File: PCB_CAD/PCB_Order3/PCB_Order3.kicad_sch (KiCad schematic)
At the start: 93 parts, among them J1 Conn_01x03_Socket, SW1 SLW-883935-2A-D

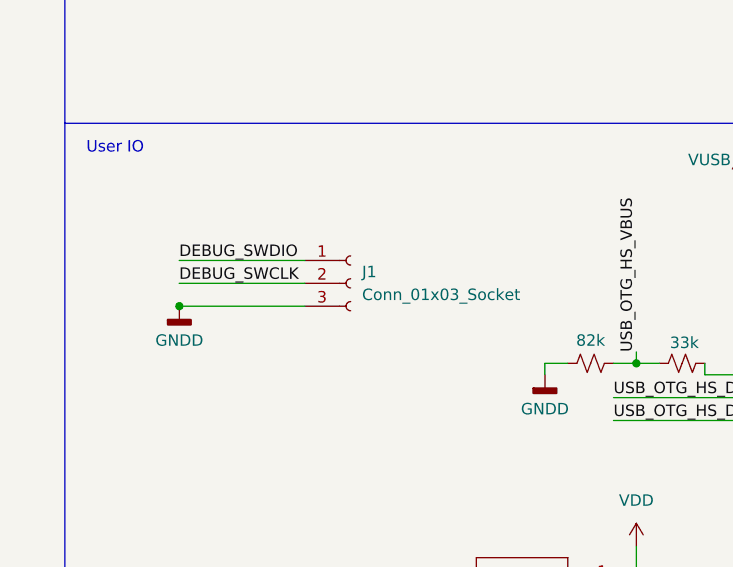
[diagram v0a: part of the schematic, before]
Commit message: preserve current PCB state, substantively ready to go to fab but messy on small details
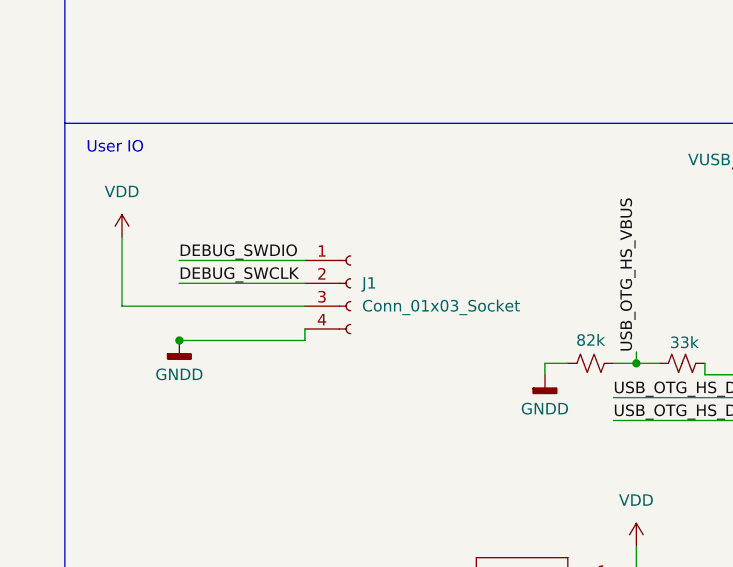
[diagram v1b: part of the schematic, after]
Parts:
- DacOut_L_decouple1, DacOut_R_decouple1: footprint Capacitor_SMD:C_0805_2012Metric_Pad1.18x1.45mm_HandSolder -> Capacitor_THT:C_Rect_L4.0mm_W2.5mm_P2.50mm
- J1: footprint Connector_PinSocket_2.54mm:PinSocket_1x03_P2.54mm_Vertical -> Connector_PinSocket_2.54mm:PinSocket_1x04_P2.54mm_Vertical; symbol Connector:Conn_01x03_Socket -> Connector:Conn_01x04_Socket
- PEC3: footprint Capacitor_SMD:C_0805_2012Metric_Pad1.18x1.45mm_HandSolder -> Capacitor_THT:CP_Radial_D6.3mm_P2.50mm
- TOSLINKL1: footprint Inductor_SMD:L_10.4x10.4_H4.8 -> Inductor_SMD:L_1812_4532Metric_Pad1.30x3.40mm_HandSolder
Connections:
- net GNDD: now also J1.4 (Pin_4); no longer J1.3 (Pin_3)
- net VDD: now also J1.3 (Pin_3)
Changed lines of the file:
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@@
 	)
 	(junction
-		(at 218.4627 307.34)
-		(diameter 0)
-		(color 0 0 0 0)
-	)
-	(junction
 		(at 280.67 314.96)
 		(diameter 0)
@@
 	)
 	(junction
+		(at 218.4627 311.15)
+		(diameter 0)
+		(color 0 0 0 0)
+	)
+	(junction
 		(at 241.3 115.57)
 		(diameter 0)
@@
 	(wire
 		(pts
+			(xy 232.41 307.34) (xy 212.09 307.34)
+		)
+		(stroke
+			(width 0)
+			(type default)
+		)
+	)
+	(wire
+		(pts
 			(xy 596.9 248.92) (xy 596.9 252.73)
 		)
@@
 	(wire
 		(pts
+			(xy 232.41 311.15) (xy 232.41 309.88)
+		)
+		(stroke
+			(width 0)
+			(type default)
+		)
+	)
+	(wire
+		(pts
 			(xy 386.08 297.18) (xy 398.78 297.18)
 		)
@@
 	(wire
 		(pts
-			(xy 218.4627 307.34) (xy 232.41 307.34)
-		)
-		(stroke
-			(width 0)
-			(type default)
-		)
-	)
-	(wire
-		(pts
 			(xy 440.69 133.35) (xy 449.58 133.35)
 		)
@@
 	(wire
 		(pts
+			(xy 218.44 311.15) (xy 218.4627 311.15)
+		)
+		(stroke
+			(width 0)
+			(type default)
+		)
+	)
+	(wire
+		(pts
 			(xy 364.49 353.06) (xy 364.49 347.98)
 		)
@@
 	(wire
 		(pts
+			(xy 218.4627 311.15) (xy 232.41 311.15)
+		)
+		(stroke
+			(width 0)
+			(type default)
+		)
+	)
+	(wire
+		(pts
 			(xy 318.77 340.36) (xy 321.31 340.36)
 		)
@@
 	(wire
 		(pts
+			(xy 212.09 307.34) (xy 212.09 299.72)
+		)
+		(stroke
+			(width 0)
+			(type default)
+		)
+	)
+	(wire
+		(pts
 			(xy 596.9 248.92) (xy 618.49 248.92)
 		)
@@
 	(wire
 		(pts
-			(xy 218.44 307.34) (xy 218.4627 307.34)
-		)
-		(stroke
-			(width 0)
-			(type default)
-		)
-	)
-	(wire
-		(pts
 			(xy 227.33 148.59) (xy 233.68 148.59)
 		)
@@
 			)
 		)
-		(property "Footprint" "Capacitor_SMD:C_0805_2012Metric_Pad1.18x1.45mm_HandSolder"
+		(property "Footprint" "Capacitor_THT:C_Rect_L4.0mm_W2.5mm_P2.50mm"
 			(at 648.97 257.81 0)
 			(effects
@@
 			)
 		)
-		(property "Footprint" "Capacitor_SMD:C_0805_2012Metric_Pad1.18x1.45mm_HandSolder"
+		(property "Footprint" "Capacitor_THT:C_Rect_L4.0mm_W2.5mm_P2.50mm"
 			(at 642.62 256.54 0)
 			(effects
@@
 			)
 		)
-		(property "Footprint" "Capacitor_SMD:C_0805_2012Metric_Pad1.18x1.45mm_HandSolder"
+		(property "Footprint" "Capacitor_THT:CP_Radial_D6.3mm_P2.50mm"
 			(at 251.46 113.03 0)
 			(effects
@@
 	)
 	(symbol
+		(lib_id "power:VDD")
+		(at 212.09 299.72 0)
+		(unit 1)
+		(exclude_from_sim no)
+		(in_bom yes)
+		(on_board yes)
+		(dnp no)
+		(fields_autoplaced yes)
+		(property "Reference" "#PWR049"
+			(at 212.09 303.53 0)
+			(effects
+				(font
+					(size 1.27 1.27)
+				)
+				(hide yes)
+			)
+		)
+		(property "Value" "VDD"
+			(at 212.09 294.64 0)
+			(effects
+				(font
+					(size 1.27 1.27)
+				)
+			)
+		)
+		(property "Footprint" ""
+			(at 212.09 299.72 0)
+			(effects
+				(font
+					(size 1.27 1.27)
+				)
+				(hide yes)
+			)
+		)
+		(property "Datasheet" ""
+			(at 212.09 299.72 0)
+			(effects
+				(font
+					(size 1.27 1.27)
+				)
+				(hide yes)
+			)
+		)
+		(property "Description" "Power symbol creates a global label with name \"VDD\""
+			(at 212.09 299.72 0)
+			(effects
+				(font
+					(size 1.27 1.27)
+				)
+				(hide yes)
+			)
+		)
+		(pin "1"
+		)
+		(instances
+			(project ""
+				(path "/85a2a93a-53e0-46c8-b7f5-ee661b6f3053"
+					(reference "#PWR049")
+					(unit 1)
+				)
+			)
+		)
+	)
+	(symbol
 		(lib_id "Device:C_Small")
 		(at 497.84 358.14 90)
@@
 	(symbol
 		(lib_id "power:GNDD")
-		(at 218.4627 307.34 0)
+		(at 218.4627 311.15 0)
 		(unit 1)
 		(exclude_from_sim no)
@@
 		(fields_autoplaced yes)
 		(property "Reference" "#PWR0104"
-			(at 218.4627 313.69 0)
+			(at 218.4627 317.5 0)
 			(effects
 				(font
@@
 		)
 		(property "Value" "GNDD"
-			(at 218.4627 311.15 0)
+			(at 218.4627 314.96 0)
 			(effects
 				(font
@@
 		)
 		(property "Footprint" ""
-			(at 218.4627 307.34 0)
+			(at 218.4627 311.15 0)
 			(effects
 				(font
@@
 		)
 		(property "Datasheet" ""
-			(at 218.4627 307.34 0)
+			(at 218.4627 311.15 0)
 			(effects
 				(font
@@
 		)
 		(property "Description" "Power symbol creates a global label with name \"GNDD\" , digital ground"
-			(at 218.4627 307.34 0)
+			(at 218.4627 311.15 0)
 			(effects
 				(font
@@
 	)
 	(symbol
-		(lib_id "Connector:Conn_01x03_Socket")
+		(lib_id "Connector:Conn_01x04_Socket")
 		(at 237.49 304.8 0)
 		(unit 1)
@@
 		(fields_autoplaced yes)
 		(property "Reference" "J1"
-			(at 238.76 303.5299 0)
+			(at 238.76 304.7999 0)
 			(effects
 				(font
@@
 		)
 		(property "Value" "Conn_01x03_Socket"
-			(at 238.76 306.0699 0)
+			(at 238.76 307.3399 0)
 			(effects
 				(font
@@
 			)
 		)
-		(property "Footprint" "Connector_PinSocket_2.54mm:PinSocket_1x03_P2.54mm_Vertical"
+		(property "Footprint" "Connector_PinSocket_2.54mm:PinSocket_1x04_P2.54mm_Vertical"
 			(at 237.49 304.8 0)
 			(effects
@@
 			)
 		)
-		(property "Description" "Generic connector, single row, 01x03, script generated"
+		(property "Description" "Generic connector, single row, 01x04, script generated"
 			(at 237.49 304.8 0)
 			(effects
@@
 		(pin "2"
 		)
+		(pin "4"
+		)
 		(instances
 			(project ""
@@
 			)
 		)
-		(property "Footprint" "Inductor_SMD:L_10.4x10.4_H4.8"
+		(property "Footprint" "Inductor_SMD:L_1812_4532Metric_Pad1.30x3.40mm_HandSolder"
 			(at 557.53 101.6 0)
 			(effects
